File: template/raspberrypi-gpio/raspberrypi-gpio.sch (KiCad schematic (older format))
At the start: 1 part, among them P1 CONN_13X2

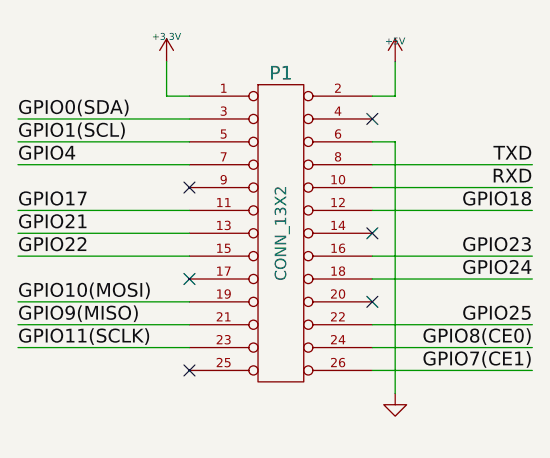
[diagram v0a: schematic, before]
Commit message: fix template
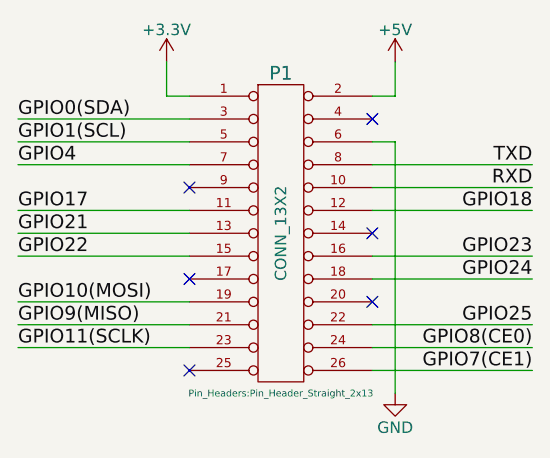
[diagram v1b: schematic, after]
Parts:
- P1: footprint (none) -> Pin_Headers:Pin_Header_Straight_2x13
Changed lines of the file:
@@
-EESchema Schematic File Version 2  date 15/11/2012 21:22:43
+EESchema Schematic File Version 2
 LIBS:power
 LIBS:device
@@
 LIBS:memory
 LIBS:xilinx
-LIBS:special
 LIBS:microcontrollers
 LIBS:dsp
@@
 LIBS:audio
 LIBS:interface
-LIBS:digital-audio
-LIBS:philips
-LIBS:display
-LIBS:cypress
-LIBS:siliconi
 LIBS:opto
-LIBS:atmel
-LIBS:contrib
-LIBS:valves
-LIBS:rpi-cache
-EELAYER 27 0
+LIBS:raspberrypi-gpio-cache
+EELAYER 25 0
 EELAYER END
 $Descr A4 11693 8268
@@
 F 0 "P1" H 2400 2500 60  0000 C CNN
 F 1 "CONN_13X2" V 2400 1800 50  0000 C CNN
+F 2 "Pin_Headers:Pin_Header_Straight_2x13" H 2400 1100 30  0000 C CNN
+F 3 "" H 2400 1800 60  0001 C CNN
 	1    2400 1800
 	1    0    0    -1
@@
 U 1 1 50A55B18
 P 1900 1050
-F 0 "#PWR01" H 1900 1010 30  0001 C CNN
-F 1 "+3.3V" H 1900 1160 30  0000 C CNN
+F 0 "#PWR01" H 1900 900 50  0001 C CNN
+F 1 "+3.3V" H 1900 1190 50  0000 C CNN
+F 2 "" H 1900 1050 50  0000 C CNN
+F 3 "" H 1900 1050 50  0000 C CNN
 	1    1900 1050
 	1    0    0    -1
@@
 U 1 1 50A55B2E
 P 2900 1050
-F 0 "#PWR02" H 2900 1140 20  0001 C CNN
-F 1 "+5V" H 2900 1140 30  0000 C CNN
+F 0 "#PWR02" H 2900 900 50  0001 C CNN
+F 1 "+5V" H 2900 1190 50  0000 C CNN
+F 2 "" H 2900 1050 50  0000 C CNN
+F 3 "" H 2900 1050 50  0000 C CNN
 	1    2900 1050
 	1    0    0    -1
@@
 U 1 1 50A55C3F
 P 2900 2500
-F 0 "#PWR03" H 2900 2500 30  0001 C CNN
-F 1 "GND" H 2900 2430 30  0001 C CNN
+F 0 "#PWR03" H 2900 2250 50  0001 C CNN
+F 1 "GND" H 2900 2350 50  0000 C CNN
+F 2 "" H 2900 2500 50  0000 C CNN
+F 3 "" H 2900 2500 50  0000 C CNN
 	1    2900 2500
 	1    0    0    -1
